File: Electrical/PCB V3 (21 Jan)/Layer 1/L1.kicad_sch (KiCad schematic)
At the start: 218 parts, among them J1 Conn_01x05, Q1 NMOS, U1 LM2587S-ADJ, U2 CD74HC4067SM, U3 CD74HC4067SM, U4 XT30UPB-M, U5 113991054

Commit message: exported l1 step file, added some 3d models to l1, spammed save
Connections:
- net GND: now also U4.2 (-); no longer U4.P$2 (-)
- net at Q1.1 (D): now also U4.1 (+); no longer U4.P$1 (+)
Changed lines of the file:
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@@
 		)
 		(property "Footprint" "Connector_AMASS:AMASS_XT30U-M_1x02_P5.0mm_Vertical"
-			(at 501.65 190.5 0)
+			(at 500.634 196.85 0)
 			(effects
 				(font
@@
 		)
 		(property "MF" "amass"
-			(at 501.65 190.5 0)
+			(at 501.396 196.596 0)
 			(effects
 				(font
@@
 		)
 		(property "Description_1" "\n                        \n                            Socket; DC supply; XT30; male; PIN: 2; on PCBs; THT; yellow; 15A; 500V\n                        \n"
-			(at 501.65 190.5 0)
+			(at 500.634 196.85 0)
 			(effects
 				(font
@@
 		)
 		(property "Package" "None"
-			(at 501.65 190.5 0)
+			(at 501.904 195.834 0)
 			(effects
 				(font
@@
 		)
 		(property "Price" "None"
-			(at 501.65 190.5 0)
+			(at 501.65 196.596 0)
 			(effects
 				(font
@@
 		)
 		(property "SnapEDA_Link" "https://www.snapeda.com/parts/XT30UPB-M/AMASS/view-part/?ref=snap"
-			(at 501.65 190.5 0)
+			(at 501.396 196.596 0)
 			(effects
 				(font
@@
 		)
 		(property "MP" "XT30UPB-M"
-			(at 501.65 190.5 0)
+			(at 500.634 196.85 0)
 			(effects
 				(font
@@
 		)
 		(property "Availability" "Not in stock"
-			(at 501.65 190.5 0)
+			(at 501.142 195.58 0)
 			(effects
 				(font
@@
 		)
 		(property "Check_prices" "https://www.snapeda.com/parts/XT30UPB-M/AMASS/view-part/?ref=eda"
-			(at 501.65 190.5 0)
+			(at 501.142 196.088 0)
 			(effects
 				(font
@@
 			)
 		)
-		(pin "P$2"
+		(pin "2"
 		)
-		(pin "P$1"
+		(pin "1"
 		)
 		(instances

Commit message: 2 new jsts
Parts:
- removed J1: Conn_01x05, Connector_JST:JST_EH_B5B-EH-A_1x05_P2.50mm_Vertical, symbol Connector_Generic:Conn_01x05
- added J1: Conn_01x04, Connector_JST:JST_EH_B4B-EH-A_1x04_P2.50mm_Vertical, symbol Connector_Generic:Conn_01x04
- added J2: Conn_01x02, Connector_JST:JST_EH_B2B-EH-A_1x02_P2.50mm_Vertical, symbol Connector_Generic:Conn_01x02
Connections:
- net +12V: now also J2.2 (Pin_2)
- net +3V3: now also J1.4 (Pin_4)
- net GND: now also J1.1 (Pin_1), J2.1 (Pin_1)
- net L1 RX: now also J1.3 (Pin_3)
- net L1 TX: now also J1.2 (Pin_2)
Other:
- note added: "Power (12V & GND)"
- note removed: "Power (12v)"

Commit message: redid l1
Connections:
- net +24V: no longer D1.2 (A)
- net GND: now also D1.2 (A); no longer D1.1 (K)
- net at Q1.1 (D), U4.1 (+): now also D1.1 (K)
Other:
- moved on the sheet: D1, U4

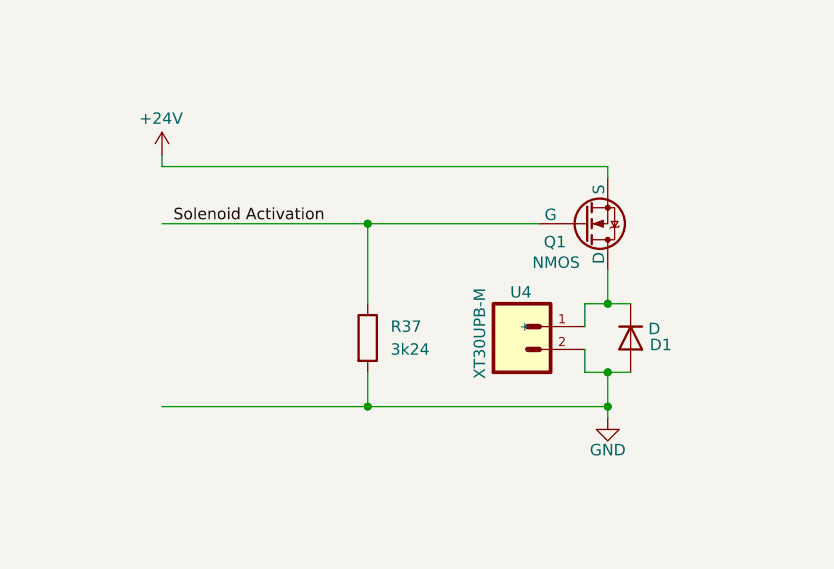
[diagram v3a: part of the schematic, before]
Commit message: fixed diode and activation cirucit for solenoid (l1), exported step files of all layers
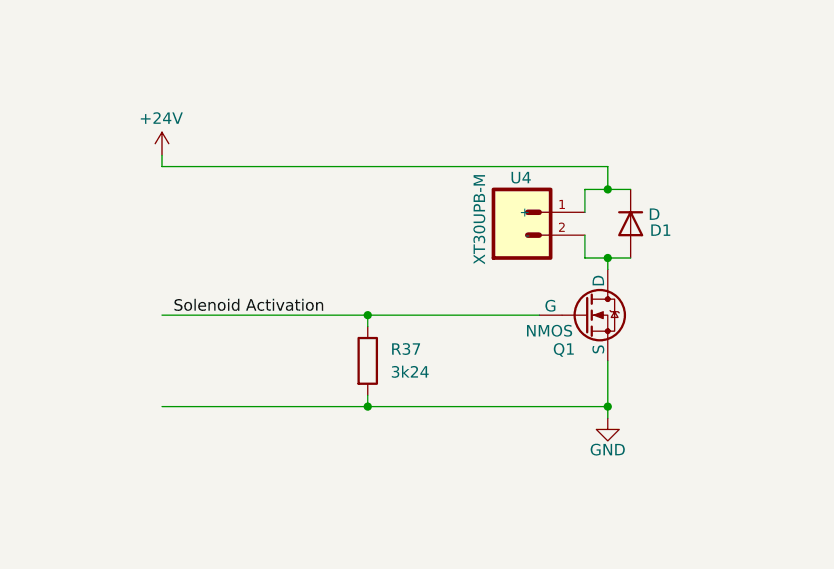
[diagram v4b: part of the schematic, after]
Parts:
- D1: footprint Diode_SMD:D_0603_1608Metric -> Diode_THT:D_DO-201AD_P15.24mm_Horizontal
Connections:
- net +24V: now also D1.1 (K), U4.1 (+); no longer Q1.3 (S)
- net GND: now also Q1.3 (S); no longer D1.2 (A), U4.2 (-)
- new net: D1.2 (A), Q1.1 (D), U4.2 (-)
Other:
- moved on the sheet: D1, Q1, R37, U4
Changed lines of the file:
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@@
 	)
 	(junction
-		(at 483.87 176.53)
-		(diameter 0)
-		(color 0 0 0 0)
-	)
-	(junction
 		(at 111.76 95.25)
 		(diameter 0)
@@
 	)
 	(junction
-		(at 510.54 185.42)
+		(at 510.54 172.72)
 		(diameter 0)
 		(color 0 0 0 0)
@@
 	)
 	(junction
+		(at 483.87 186.69)
+		(diameter 0)
+		(color 0 0 0 0)
+	)
+	(junction
 		(at 215.9 57.15)
 		(diameter 0)
@@
 	)
 	(junction
-		(at 510.54 193.04)
-		(diameter 0)
-		(color 0 0 0 0)
-	)
-	(junction
 		(at 250.19 142.24)
 		(diameter 0)
@@
 	)
 	(junction
+		(at 510.54 180.34)
+		(diameter 0)
+		(color 0 0 0 0)
+	)
+	(junction
 		(at 139.7 64.77)
 		(diameter 0)
@@
 	(wire
 		(pts
-			(xy 510.54 170.18) (xy 510.54 171.45)
+			(xy 510.54 170.18) (xy 510.54 172.72)
 		)
 		(stroke
@@
 	(wire
 		(pts
+			(xy 510.54 180.34) (xy 513.08 180.34)
+		)
+		(stroke
+			(width 0)
+			(type default)
+		)
+	)
+	(wire
+		(pts
 			(xy 111.76 67.31) (xy 119.38 67.31)
 		)
@@
 	(wire
 		(pts
-			(xy 508 193.04) (xy 510.54 193.04)
+			(xy 508 180.34) (xy 510.54 180.34)
 		)
 		(stroke
@@
 	(wire
 		(pts
-			(xy 508 193.04) (xy 508 190.5)
+			(xy 508 180.34) (xy 508 177.8)
 		)
 		(stroke
@@
 	(wire
 		(pts
-			(xy 510.54 181.61) (xy 510.54 185.42)
-		)
-		(stroke
-			(width 0)
-			(type default)
-		)
-	)
-	(wire
-		(pts
 			(xy 363.22 163.83) (xy 363.22 162.56)
 		)
@@
 	(wire
 		(pts
-			(xy 483.87 185.42) (xy 483.87 176.53)
+			(xy 483.87 187.96) (xy 483.87 186.69)
 		)
 		(stroke
@@
 	(wire
 		(pts
-			(xy 461.01 176.53) (xy 483.87 176.53)
+			(xy 461.01 186.69) (xy 483.87 186.69)
 		)
 		(stroke
@@
 	(wire
 		(pts
-			(xy 510.54 193.04) (xy 513.08 193.04)
-		)
-		(stroke
-			(width 0)
-			(type default)
-		)
-	)
-	(wire
-		(pts
 			(xy 257.81 142.24) (xy 260.35 142.24)
 		)
@@
 	(wire
 		(pts
-			(xy 510.54 185.42) (xy 513.08 185.42)
+			(xy 510.54 172.72) (xy 513.08 172.72)
 		)
 		(stroke
@@
 	(wire
 		(pts
-			(xy 483.87 196.85) (xy 483.87 193.04)
+			(xy 483.87 196.85) (xy 483.87 195.58)
 		)
 		(stroke
@@
 	(wire
 		(pts
-			(xy 508 185.42) (xy 510.54 185.42)
+			(xy 508 172.72) (xy 510.54 172.72)
 		)
 		(stroke
@@
 	(wire
 		(pts
-			(xy 508 185.42) (xy 508 187.96)
+			(xy 508 172.72) (xy 508 175.26)
 		)
 		(stroke
@@
 	(wire
 		(pts
-			(xy 510.54 196.85) (xy 510.54 193.04)
+			(xy 510.54 196.85) (xy 510.54 191.77)
 		)
 		(stroke
@@
 	(wire
 		(pts
-			(xy 483.87 176.53) (xy 502.92 176.53)
+			(xy 483.87 186.69) (xy 502.92 186.69)
 		)
 		(stroke
@@
 	(wire
 		(pts
+			(xy 510.54 180.34) (xy 510.54 181.61)
+		)
+		(stroke
+			(width 0)
+			(type default)
+		)
+	)
+	(wire
+		(pts
 			(xy 415.29 53.34) (xy 415.29 69.85)
 		)
@@
 	)
 	(label "Solenoid Activation"
-		(at 462.28 176.53 0)
+		(at 462.28 186.69 0)
 		(effects
 			(font
@@
 	(symbol
 		(lib_id "Simulation_SPICE:NMOS")
-		(at 508 176.53 0)
-		(mirror x)
+		(at 508 186.69 0)
 		(unit 1)
 		(exclude_from_sim no)
@@
 		(dnp no)
 		(property "Reference" "Q1"
-			(at 503.428 178.562 0)
+			(at 504.444 190.5 0)
 			(effects
 				(font
@@
 		)
 		(property "Value" "NMOS"
-			(at 502.158 180.848 0)
+			(at 501.396 188.468 0)
 			(effects
 				(font
@@
 		)
 		(property "Footprint" "Package_TO_SOT_THT:TO-220-3_Vertical"
-			(at 513.08 179.07 0)
+			(at 513.08 184.15 0)
 			(effects
 				(font
@@
 		)
 		(property "Datasheet" "https://ngspice.sourceforge.io/docs/ngspice-html-manual/manual.xhtml#cha_MOSFETs"
-			(at 508 163.83 0)
+			(at 508 199.39 0)
 			(effects
 				(font
@@
 		)
 		(property "Description" "N-MOSFET transistor, drain/source/gate"
-			(at 508 176.53 0)
+			(at 508 186.69 0)
 			(effects
 				(font
@@
 		)
 		(property "Sim.Device" "NMOS"
-			(at 508 159.385 0)
+			(at 508 203.835 0)
 			(effects
 				(font
@@
 		)
 		(property "Sim.Type" "VDMOS"
-			(at 508 157.48 0)
+			(at 508 205.74 0)
 			(effects
 				(font
@@
 		)
 		(property "Sim.Pins" "1=D 2=G 3=S"
-			(at 508 161.29 0)
+			(at 508 201.93 0)
 			(effects
 				(font
@@
 	(symbol
 		(lib_id "amass xt 30:XT30UPB-M")
-		(at 500.38 190.5 0)
+		(at 500.38 177.8 0)
 		(unit 1)
 		(exclude_from_sim no)
@@
 		(dnp no)
 		(property "Reference" "U4"
-			(at 500.888 184.15 0)
+			(at 500.888 171.45 0)
 			(effects
 				(font
@@
 		)
 		(property "Value" "XT30UPB-M"
-			(at 496.316 188.722 90)
+			(at 496.316 176.022 90)
 			(effects
 				(font
@@
 		)
 		(property "Footprint" "Connector_AMASS:AMASS_XT30U-M_1x02_P5.0mm_Vertical"
-			(at 499.364 196.85 0)
+			(at 499.364 184.15 0)
 			(effects
 				(font
@@
 		)
 		(property "Datasheet" ""
-			(at 500.38 190.5 0)
+			(at 500.38 177.8 0)
 			(effects
 				(font
@@
 		)
 		(property "Description" ""
-			(at 500.38 190.5 0)
+			(at 500.38 177.8 0)
 			(effects
 				(font
@@
 		)
 		(property "MF" "amass"
-			(at 500.126 196.596 0)
+			(at 500.126 183.896 0)
 			(effects
 				(font
@@
 		)
 		(property "Description_1" "\n                        \n                            Socket; DC supply; XT30; male; PIN: 2; on PCBs; THT; yellow; 15A; 500V\n                        \n"
-			(at 499.364 196.85 0)
+			(at 499.364 184.15 0)
 			(effects
 				(font
@@
 		)
 		(property "Package" "None"
-			(at 500.634 195.834 0)
+			(at 500.634 183.134 0)
 			(effects
 				(font
@@
 		)
 		(property "Price" "None"
-			(at 500.38 196.596 0)
+			(at 500.38 183.896 0)
 			(effects
 				(font
@@
 		)
 		(property "SnapEDA_Link" "https://www.snapeda.com/parts/XT30UPB-M/AMASS/view-part/?ref=snap"
-			(at 500.126 196.596 0)
+			(at 500.126 183.896 0)
 			(effects
 				(font
@@
 		)
 		(property "MP" "XT30UPB-M"
-			(at 499.364 196.85 0)
+			(at 499.364 184.15 0)
 			(effects
 				(font
@@
 		)
 		(property "Availability" "Not in stock"
-			(at 499.872 195.58 0)
+			(at 499.872 182.88 0)
 			(effects
 				(font
@@
 		)
 		(property "Check_prices" "https://www.snapeda.com/parts/XT30UPB-M/AMASS/view-part/?ref=eda"
-			(at 499.872 196.088 0)
+			(at 499.872 183.388 0)
 			(effects
 				(font
@@
 	(symbol
 		(lib_id "Device:R")
-		(at 483.87 189.23 0)
+		(at 483.87 191.77 0)
 		(unit 1)
 		(exclude_from_sim no)
@@
 		(fields_autoplaced yes)
 		(property "Reference" "R37"
-			(at 486.41 187.9599 0)
+			(at 486.41 190.4999 0)
 			(effects
 				(font
@@
 		)
 		(property "Value" "3k24"
-			(at 486.41 190.4999 0)
+			(at 486.41 193.0399 0)
 			(effects
 				(font
@@
 		)
 		(property "Footprint" "Capacitor_SMD:C_0603_1608Metric"
-			(at 482.092 189.23 90)
+			(at 482.092 191.77 90)
 			(effects
 				(font
@@
 		)
 		(property "Datasheet" "~"
-			(at 483.87 189.23 0)
+			(at 483.87 191.77 0)
 			(effects
 				(font
@@
 		)
 		(property "Description" "Resistor"
-			(at 483.87 189.23 0)
+			(at 483.87 191.77 0)
 			(effects
 				(font
@@
 	(symbol
 		(lib_id "Device:D")
-		(at 513.08 189.23 270)
+		(at 513.08 176.53 270)
 		(unit 1)
 		(exclude_from_sim no)
@@
 		(dnp no)
 		(property "Reference" "D1"
-			(at 517.652 189.992 90)
+			(at 517.652 177.292 90)
 			(effects
 				(font
@@
 		)
 		(property "Value" "D"
-			(at 516.382 188.214 90)
+			(at 516.382 175.514 90)
 			(effects
 				(font
@@
 			)
 		)
-		(property "Footprint" "Diode_SMD:D_0603_1608Metric"
-			(at 513.08 189.23 0)
+		(property "Footprint" "Diode_THT:D_DO-201AD_P15.24mm_Horizontal"
+			(at 513.08 176.53 0)
 			(effects
 				(font
@@
 		)
 		(property "Datasheet" "~"
-			(at 513.08 189.23 0)
+			(at 513.08 176.53 0)
 			(effects
 				(font
@@
 		)
 		(property "Description" "Diode"
-			(at 513.08 189.23 0)
+			(at 513.08 176.53 0)
 			(effects
 				(font
@@
 		)
 		(property "Sim.Device" "D"
-			(at 513.08 189.23 0)
+			(at 513.08 176.53 0)
 			(effects
 				(font
@@
 		)
 		(property "Sim.Pins" "1=K 2=A"
-			(at 513.08 189.23 0)
+			(at 513.08 176.53 0)
 			(effects
 				(font

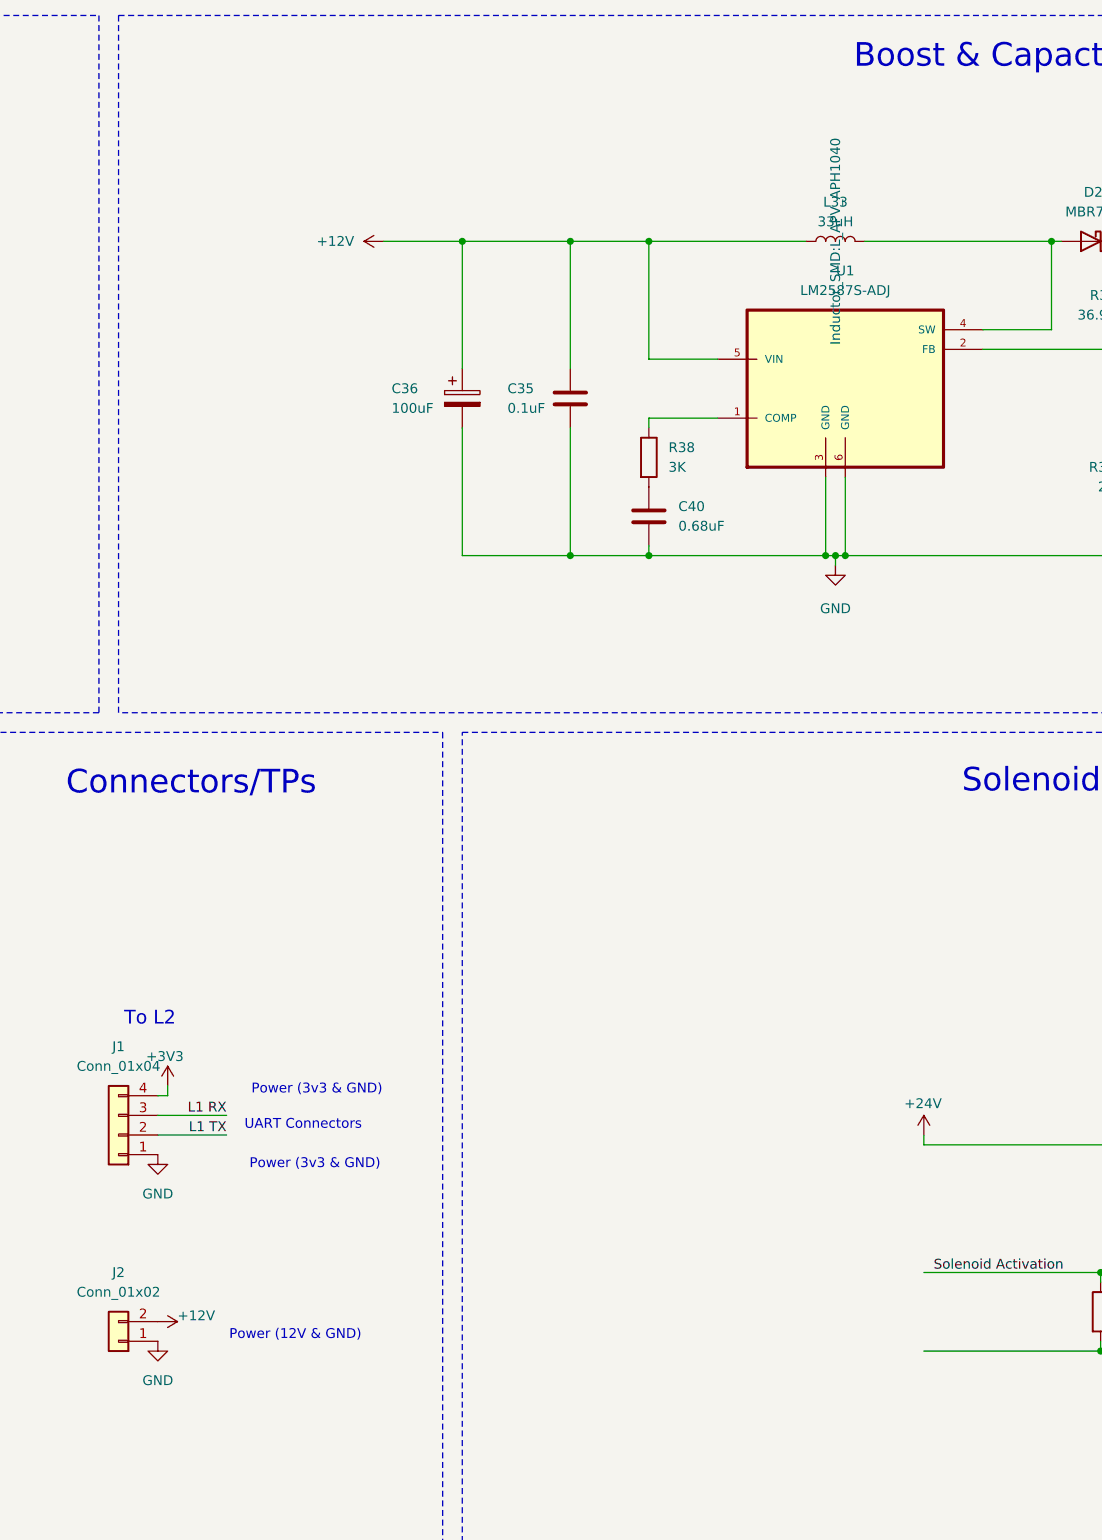
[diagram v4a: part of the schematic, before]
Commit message: removed led ring silkscreen for l1, switch 12v jst to xt30
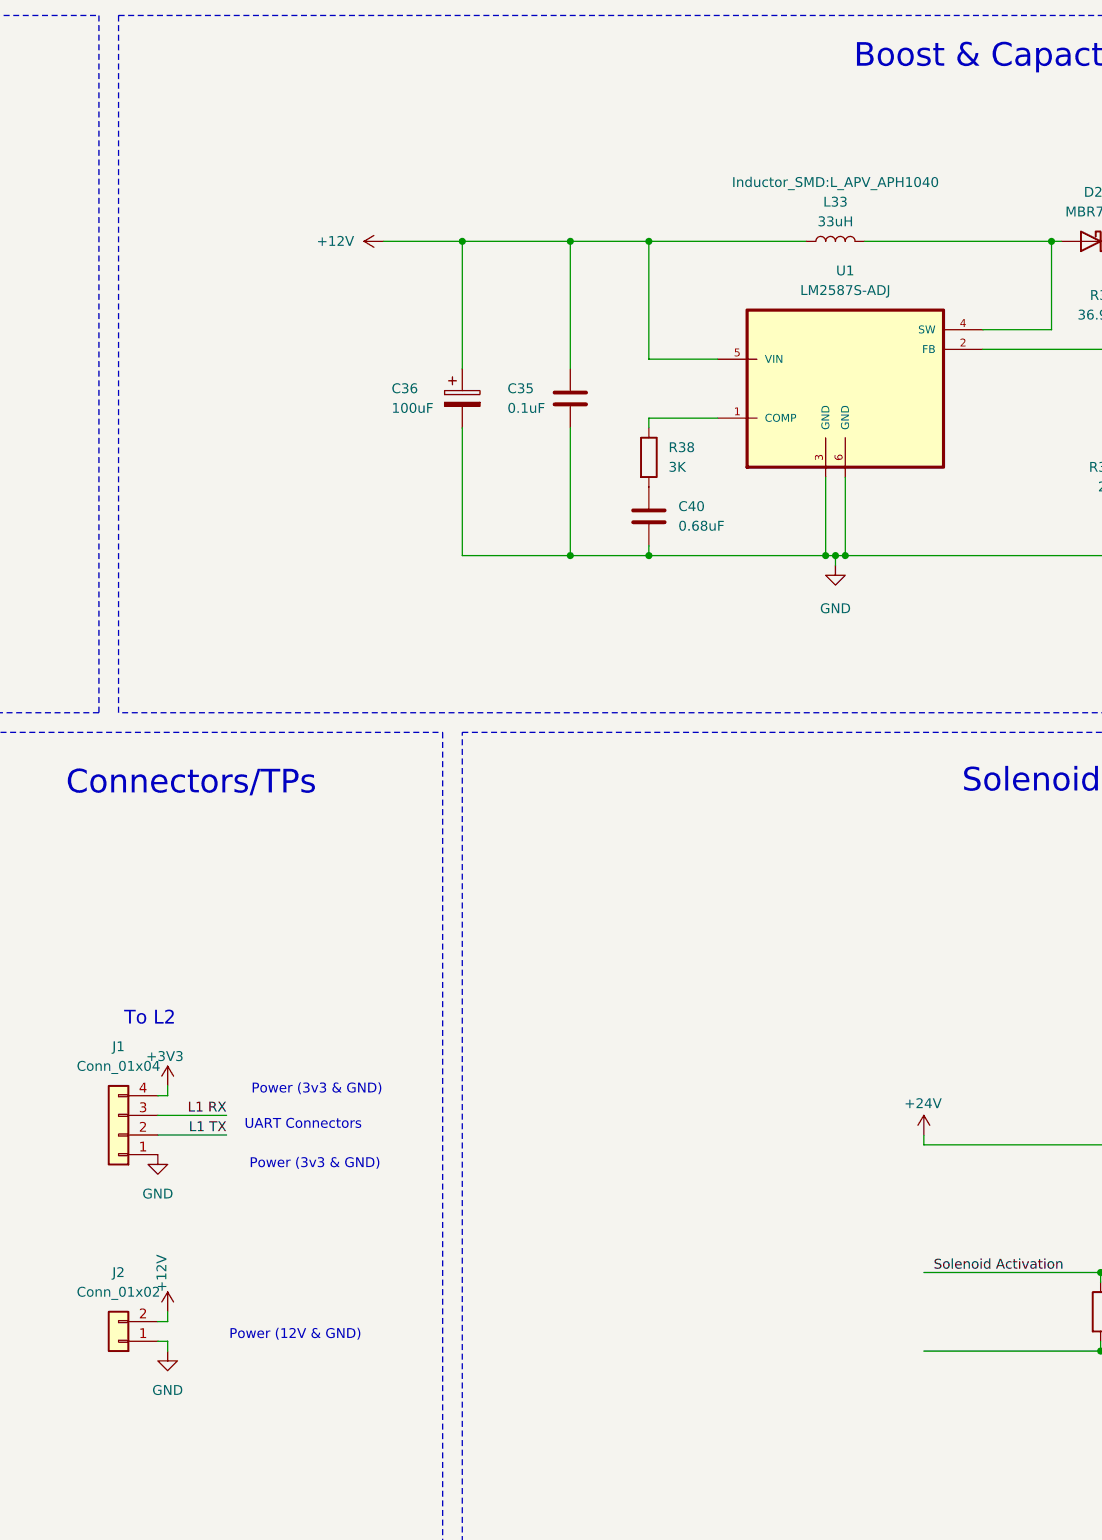
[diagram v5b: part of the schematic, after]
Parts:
- J2: footprint Connector_JST:JST_EH_B2B-EH-A_1x02_P2.50mm_Vertical -> Connector_AMASS:AMASS_XT30UPB-M_1x02_P5.0mm_Vertical
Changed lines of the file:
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@@
 	(wire
 		(pts
+			(xy 363.22 195.58) (xy 363.22 196.85)
+		)
+		(stroke
+			(width 0)
+			(type default)
+		)
+	)
+	(wire
+		(pts
 			(xy 119.38 95.25) (xy 128.27 95.25)
 		)
@@
 	(wire
 		(pts
+			(xy 363.22 195.58) (xy 361.95 195.58)
+		)
+		(stroke
+			(width 0)
+			(type default)
+		)
+	)
+	(wire
+		(pts
 			(xy 73.66 64.77) (xy 78.74 64.77)
 		)
@@
 	(wire
 		(pts
+			(xy 363.22 191.77) (xy 363.22 193.04)
+		)
+		(stroke
+			(width 0)
+			(type default)
+		)
+	)
+	(wire
+		(pts
 			(xy 496.57 93.98) (xy 487.68 93.98)
 		)
@@
 	(wire
 		(pts
+			(xy 363.22 193.04) (xy 361.95 193.04)
+		)
+		(stroke
+			(width 0)
+			(type default)
+		)
+	)
+	(wire
+		(pts
 			(xy 461.01 196.85) (xy 483.87 196.85)
 		)
@@
 	(symbol
 		(lib_id "power:+12V")
-		(at 361.95 193.04 270)
+		(at 363.22 191.77 0)
 		(unit 1)
 		(exclude_from_sim no)
@@
 		(dnp no)
 		(property "Reference" "#PWR021"
-			(at 358.14 193.04 0)
+			(at 363.22 195.58 0)
 			(effects
 				(font
@@
 		)
 		(property "Value" "+12V"
-			(at 364.49 192.278 90)
+			(at 362.458 189.23 90)
 			(effects
 				(font
@@
 		)
 		(property "Footprint" ""
-			(at 361.95 193.04 0)
+			(at 363.22 191.77 0)
 			(effects
 				(font
@@
 		)
 		(property "Datasheet" ""
-			(at 361.95 193.04 0)
+			(at 363.22 191.77 0)
 			(effects
 				(font
@@
 		)
 		(property "Description" "Power symbol creates a global label with name \"+12V\""
-			(at 361.95 193.04 0)
+			(at 363.22 191.77 0)
 			(effects
 				(font
@@
 		(on_board yes)
 		(dnp no)
-		(fields_autoplaced yes)
 		(property "Reference" "L33"
 			(at 449.58 48.26 90)
@@
 		)
 		(property "Footprint" "Inductor_SMD:L_APV_APH1040"
-			(at 449.58 53.34 0)
+			(at 449.58 45.72 90)
 			(effects
 				(font
@@
 			)
 		)
-		(property "Footprint" "Connector_JST:JST_EH_B2B-EH-A_1x02_P2.50mm_Vertical"
+		(property "Footprint" "Connector_AMASS:AMASS_XT30UPB-M_1x02_P5.0mm_Vertical"
 			(at 356.87 195.58 0)
 			(effects
@@
 	(symbol
 		(lib_id "Library:GND")
-		(at 361.95 195.58 0)
+		(at 363.22 196.85 0)
 		(unit 1)
 		(exclude_from_sim no)
@@
 		(fields_autoplaced yes)
 		(property "Reference" "#PWR03"
-			(at 361.95 201.93 0)
+			(at 363.22 203.2 0)
 			(effects
 				(font
@@
 		)
 		(property "Value" "GND"
-			(at 361.95 200.66 0)
+			(at 363.22 201.93 0)
 			(effects
 				(font
@@
 		)
 		(property "Footprint" ""
-			(at 361.95 195.58 0)
+			(at 363.22 196.85 0)
 			(effects
 				(font
@@
 		)
 		(property "Datasheet" ""
-			(at 361.95 195.58 0)
+			(at 363.22 196.85 0)
 			(effects
 				(font
@@
 		)
 		(property "Description" "Power symbol creates a global label with name \"GND\" , ground"
-			(at 361.95 195.58 0)
+			(at 363.22 196.85 0)
 			(effects
 				(font
